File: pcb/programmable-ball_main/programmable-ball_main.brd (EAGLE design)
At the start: 30 x 30 mm, 30 parts, among them J1 12402012E212A, J3 B4B-ZR-SM4-TFT(LF)(SN), P1 S2B-ZR-SM4A-TF, Q1 DMG2305UX-13, U1 MDBT50Q-1MV2, U2 AP2112K-3.3TRG1, U3 MCP73832T-2ACI/OT, Y1 FC-135_32.7680KA-A0

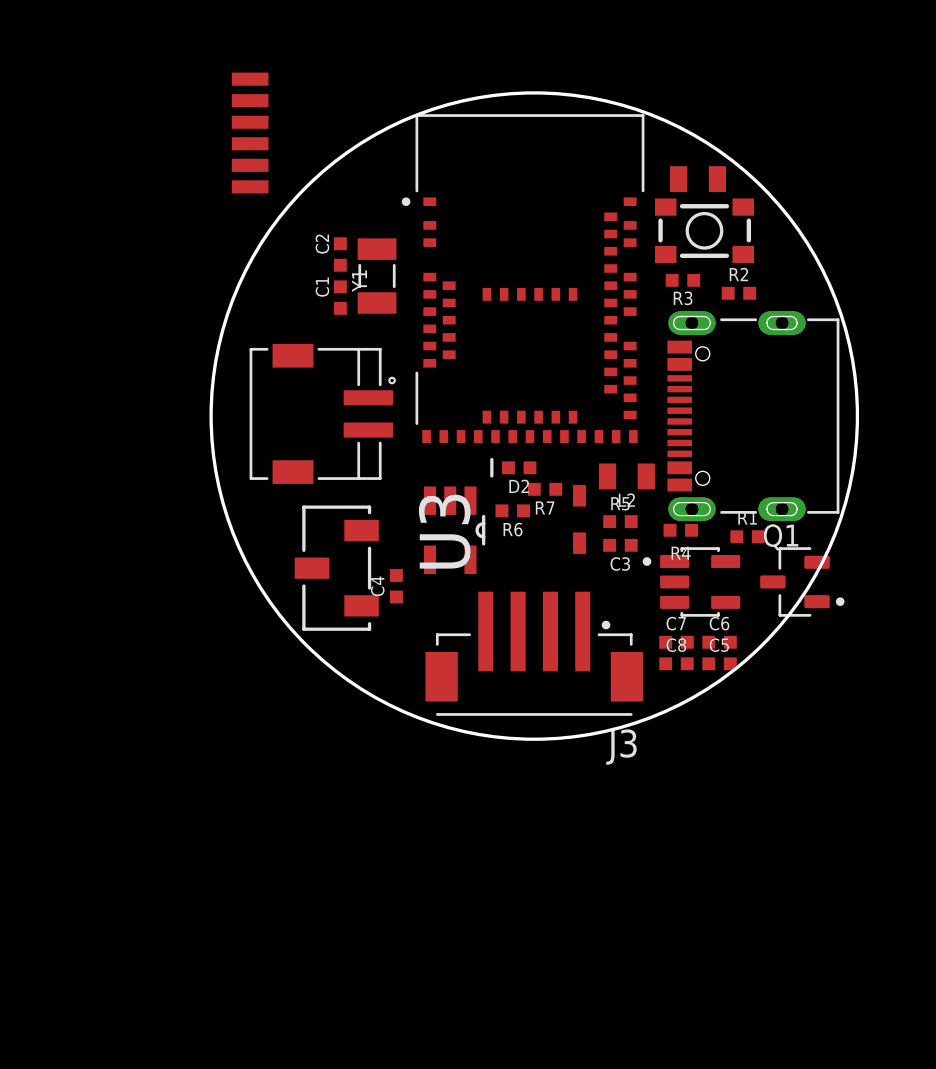
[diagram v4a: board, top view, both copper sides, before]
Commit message: 基盤外形を変更
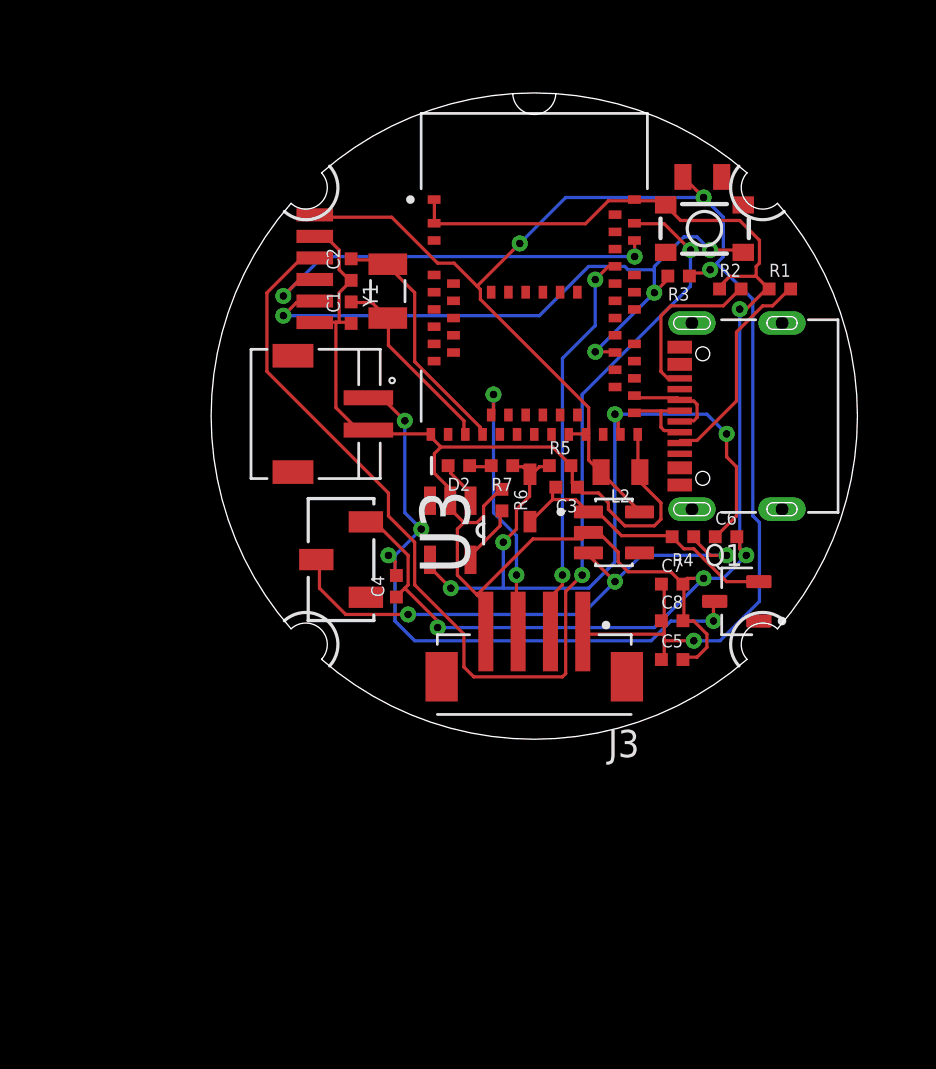
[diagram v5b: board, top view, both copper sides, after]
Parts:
- moved R1 11.6 mm to (26.4, 20.9)
- moved DNP 6.98 mm to (1.00, 21.8)
- moved C6 4.91 mm to (23.9, 9.40)
- moved U2 4.61 mm to (18.7, 9.60)
- moved R5 3.82 mm to (16.2, 12.7)
- moved C3 3.68 mm to (16.5, 11.7)
- moved Q1 2.85 mm to (24.4, 6.40)
- moved D2 2.80 mm to (11.5, 12.7)
- moved C7 2.71 mm to (21.4, 7.20)
- moved D1 2.51 mm to (14.8, 11.2)
- moved R7 2.28 mm to (13.5, 12.7)
- moved C5 2.21 mm to (21.4, 3.70)
- moved C8 2.01 mm to (21.4, 5.50)
- moved C1 0.86 mm to (6.50, 19.8)
- moved C2 0.86 mm to (6.50, 21.8)
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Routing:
- net GND: track 0.00 -> 123.7 mm, vias 0 -> 4
- net 3.3V: track 0.00 -> 71.5 mm, vias 0 -> 4
- net SWDCLK: track 0.00 -> 54.2 mm, vias 0 -> 2
- net VBUS: track 0.00 -> 36.6 mm, vias 0 -> 4
- net RESET: track 0.00 -> 32.3 mm, vias 0 -> 4
- net VBAT: track 0.00 -> 31.6 mm, vias 0 -> 4
- net EN: track 0.00 -> 25.7 mm, vias 0 -> 3
- net SWDIO: track 0.00 -> 19.6 mm, vias 0 -> 2
- net I2C_SCL: track 0.00 -> 18.4 mm, vias 0 -> 2
- net N$6: track 0.00 -> 13.3 mm
- net I2C_SDA: track 0.00 -> 12.5 mm, vias 0 -> 2
- net N$3: track 0.00 -> 11.5 mm
- net N$1: track 0.00 -> 10.0 mm
- net N$4: track 0.00 -> 8.91 mm
- net N$2: track 0.00 -> 7.82 mm
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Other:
- outline, holes or cut-outs redrawn

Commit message: 基板v1完成 resolved #4
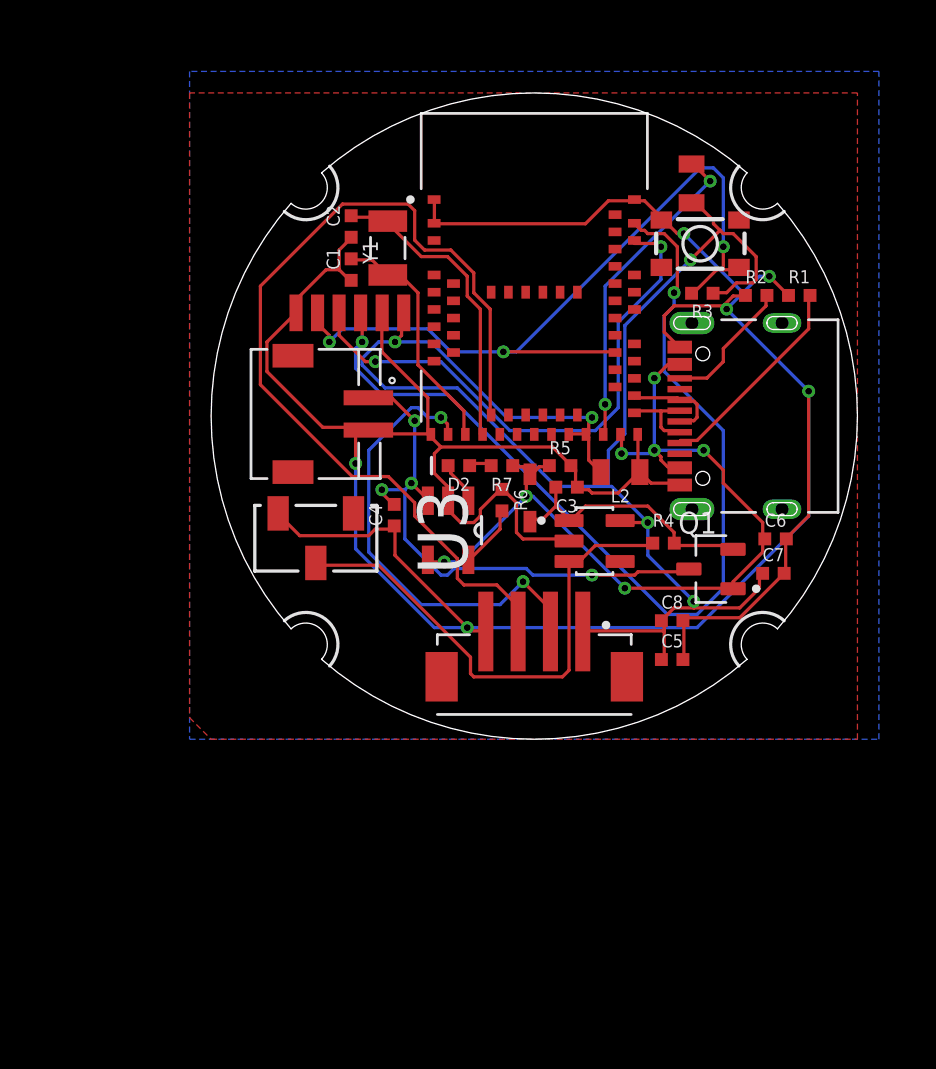
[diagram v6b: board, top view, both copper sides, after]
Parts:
- moved DNP 5.69 mm to (6.40, 23.6), turned to 0 degrees
- moved S2 4.80 mm to (7.40, 10.6), turned to 180 degrees
- moved C7 4.73 mm to (26.1, 7.70)
- moved C4 3.30 mm to (8.50, 10.4)
- moved C6 2.30 mm to (26.2, 9.30)
- moved C1 2.00 mm to (6.50, 21.8)
- moved C2 2.00 mm to (6.50, 23.8)
- moved Y1 2.00 mm to (8.20, 22.8)
- moved Q1 1.92 mm to (23.2, 7.90)
- moved R3 1.36 mm to (22.8, 20.7)
- moved R2 1.24 mm to (25.3, 20.6)
- moved U2 0.98 mm to (17.8, 9.20)
- moved R1 0.95 mm to (27.3, 20.6)
- moved R4 0.95 mm to (21.0, 9.10), turned to 0 degrees
- moved S1 0.73 mm to (22.7, 23.0)
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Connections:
- net I2C_SCL: now also U1.16; no longer U1.49
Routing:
- net I2C_SDA: track 12.5 -> 43.4 mm, vias 2 -> 0
- net GND: track 123.7 -> 151.1 mm, vias 4 -> 6
- net N$5: track 0.00 -> 15.0 mm, vias 0 -> 2
- net SWDCLK: track 54.2 -> 44.7 mm
- net SWDIO: track 19.6 -> 26.0 mm
- net VBAT: track 31.6 -> 25.7 mm
- net RESET: track 32.3 -> 36.4 mm, vias 4 -> 3
- net VBUS: track 36.6 -> 39.8 mm, vias 4 -> 7
- net I2C_SCL: track 18.4 -> 21.5 mm
- net N$3: track 11.5 -> 14.3 mm
- net N$4: track 8.91 -> 11.3 mm
- net 3.3V: track 71.5 -> 73.8 mm, vias 4 -> 5
- net EN: track 25.7 -> 23.9 mm, vias 3 -> 0
- net N$2: track 7.82 -> 6.26 mm
- net N$6: track 13.3 -> 12.3 mm
- added copper zone on layer 1, net GND
- added copper zone on layer 16, net GND
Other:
- outline, holes or cut-outs redrawn

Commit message: v1の修正
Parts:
- added R10, R11: 100k, SparkFun-Resistors:0402-TIGHT
- added R8, R9: 22Ω, SparkFun-Resistors:0402-TIGHT
- moved S2 19.5 mm to (26.8, 9.10)
- moved C7 11.9 mm to (14.3, 8.90), turned to 270 degrees
- moved C5 9.51 mm to (16.1, 11.6), turned to 270 degrees
- moved C8 8.84 mm to (15.0, 11.6), turned to 270 degrees
- moved R6 7.12 mm to (9.10, 5.50), turned to 90 degrees
- moved L2 6.87 mm to (12.6, 9.90), turned to 90 degrees
- moved C6 6.24 mm to (20.4, 11.6), turned to 270 degrees
- moved D1 5.20 mm to (10.7, 8.00), turned to 180 degrees
- moved Y1 5.10 mm to (4.00, 19.9), turned to 0 degrees
- moved U3 4.72 mm to (6.60, 8.00)
- moved R5 4.18 mm to (12.1, 11.9)
- moved Q1 3.83 mm to (22.2, 4.20), turned to 270 degrees
- moved D2 3.58 mm to (8.40, 10.9)
- moved C3 3.54 mm to (15.5, 8.30), turned to 270 degrees
- moved R7 3.49 mm to (10.1, 11.9)
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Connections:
- new net N$10: R8.1, U1.35
- new net N$11: R9.1, U1.34
- new net VDIV: R10.1, R11.2, U1.10
- net GND: now also R11.1
- net USBD+: now also R8.2; no longer U1.35
- net USBD-: now also R9.2; no longer U1.34
- net VBAT: now also R10.2
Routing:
- net GND: track 151.1 -> 0.00 mm, vias 6 -> 0
- net 3.3V: track 73.8 -> 0.00 mm, vias 5 -> 0
- net SWDCLK: track 44.7 -> 0.00 mm, vias 2 -> 0
- net I2C_SDA: track 43.4 -> 0.00 mm
- net VBUS: track 39.8 -> 0.00 mm, vias 7 -> 0
- net RESET: track 36.4 -> 0.00 mm, vias 3 -> 0
- net SWDIO: track 26.0 -> 0.00 mm, vias 2 -> 0
- net VBAT: track 25.7 -> 0.00 mm, vias 4 -> 0
- net EN: track 23.9 -> 0.00 mm
- net I2C_SCL: track 21.5 -> 0.00 mm, vias 2 -> 0
- net N$5: track 15.0 -> 0.00 mm, vias 2 -> 0
- net N$3: track 14.3 -> 0.00 mm
- net N$6: track 12.3 -> 0.00 mm
- net N$4: track 11.3 -> 0.00 mm
- net N$1: track 9.81 -> 0.00 mm
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
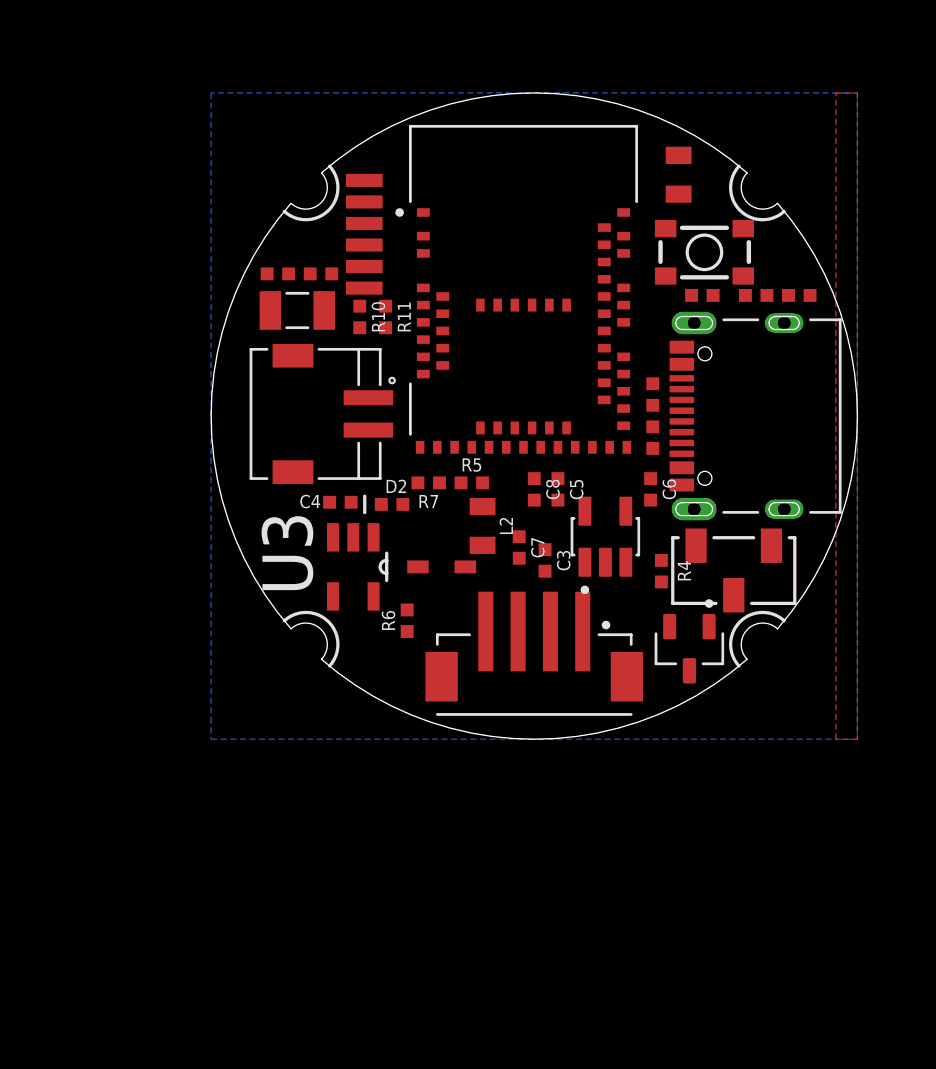
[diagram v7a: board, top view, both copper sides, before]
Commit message: パターン調整前を最新版に変更
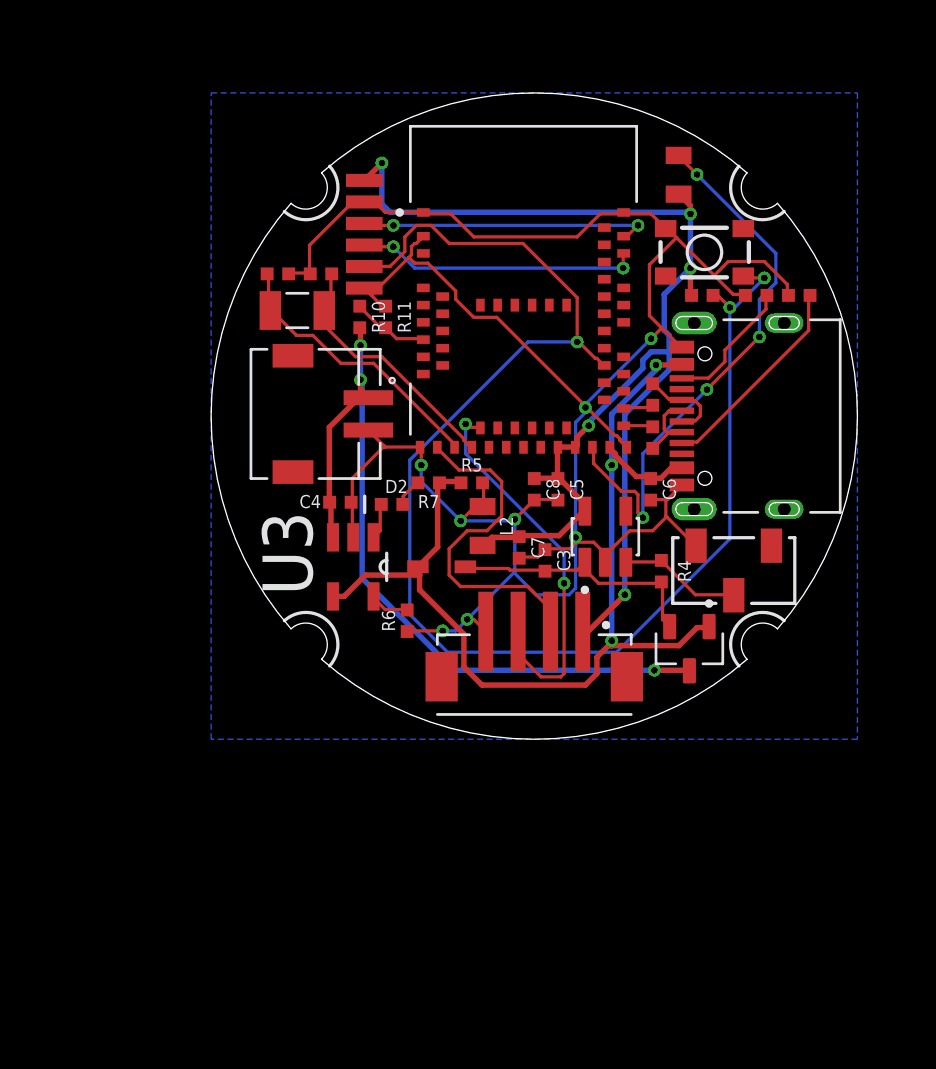
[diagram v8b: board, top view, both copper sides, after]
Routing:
- net GND: track 0.00 -> 116.6 mm, vias 0 -> 8
- net RESET: track 0.00 -> 66.1 mm, vias 0 -> 3
- net 3.3V: track 0.00 -> 59.4 mm, vias 0 -> 5
- net VBUS: track 0.00 -> 48.4 mm, vias 0 -> 3
- net VBAT: track 0.00 -> 37.3 mm, vias 0 -> 3
- net N$5: track 0.00 -> 25.8 mm, vias 0 -> 4
- net I2C_SDA: track 0.00 -> 17.9 mm, vias 0 -> 2
- net I2C_SCL: track 0.00 -> 16.0 mm
- net SWDCLK: track 0.00 -> 13.6 mm, vias 0 -> 2
- net SWDIO: track 0.00 -> 13.1 mm, vias 0 -> 2
- net N$4: track 0.00 -> 13.0 mm
- net N$6: track 0.00 -> 12.4 mm
- net N$3: track 0.00 -> 11.8 mm
- net N$1: track 0.00 -> 9.73 mm
- net N$2: track 0.00 -> 6.21 mm
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- removed copper zone on layer 1, net GND
